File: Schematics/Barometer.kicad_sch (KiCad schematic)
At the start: 4 parts, among them U6 MPL3115A2R1

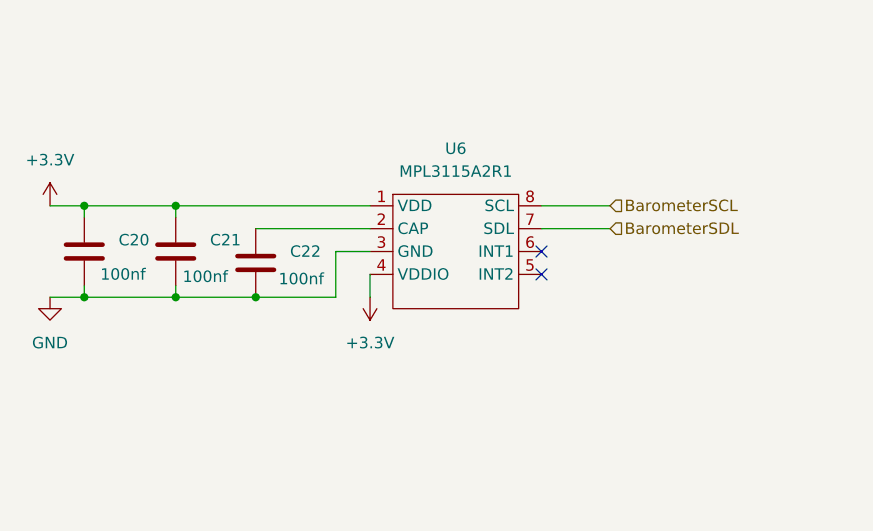
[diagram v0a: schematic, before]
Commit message: added aux pyro added reverse polarity protection re routed just need to clean up and check pin assignments
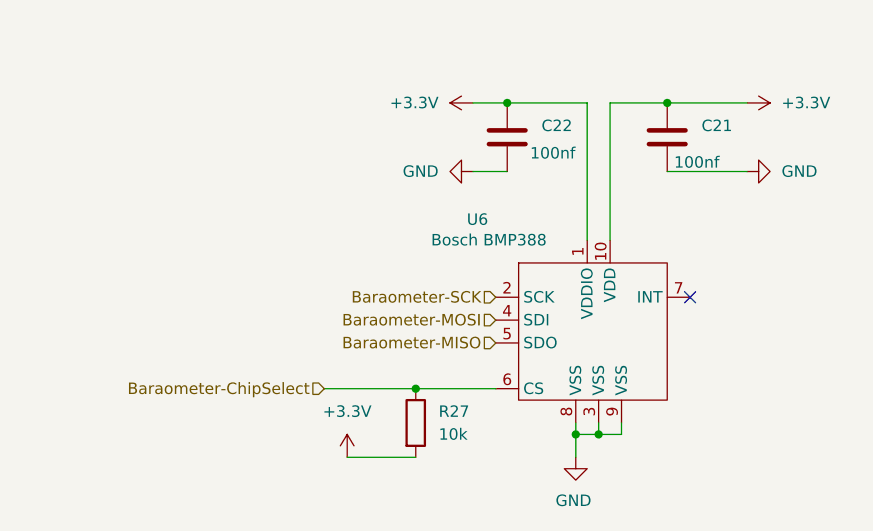
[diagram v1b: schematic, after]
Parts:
- removed C20: 100nf, Capacitor_SMD:C_0805_2012Metric_Pad1.18x1.45mm_HandSolder, symbol Device:C
- added R27: 10k, Resistor_SMD:R_0805_2012Metric_Pad1.20x1.40mm_HandSolder, symbol Device:R
- U6: value MPL3115A2R1 -> Bosch BMP388; footprint Package_LGA:LGA-8_3x5mm_P1.25mm -> myFootprints:PQFN50P200X200X80-10N; LCSC C54429 -> C779278
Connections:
- net BarometerSCL is gone; now on net GND: U6.8 (VSS)
- net +3.3V: now also C22.1, U6.10 (VDD), R27.2; no longer U6.4 (VDDIO)
- net GND: now also U6.9 (VSS)
- net Baraometer-SCK: now reaches U6.2 (SCK)
- net Baraometer-SCK: no longer C22.1
- net Baraometer-MISO: now reaches U6.5 (SDO)
- net Baraometer-ChipSelect: now reaches U6.6 (CS)
- net Baraometer-ChipSelect: now also R27.1
- net BarometerSDL: no longer names the net of U6.7 (INT)
- new net Baraometer-MOSI: U6.4 (SDI)
- no-connect marks 2 -> 1
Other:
- moved on the sheet: C21, C22

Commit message: added comments, awaiting review
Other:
- note added: "Baraometer to detect altitude and apogee events"
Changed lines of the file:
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@@
 	(generator_version "9.0")
 	(paper "A4")
+	(text "Baraometer to detect altitude and apogee events"
+		(exclude_from_sim no)
+		(at 157.48 56.896 0)
+		(effects
+			(font
+				(size 1.27 1.27)
+			)
+		)
+	)
 	(junction
 		(at 137.16 96.52)

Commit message: updated to KiCad 10.0, updated .gitignore
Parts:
- R27: LCSC C84376 -> C17414
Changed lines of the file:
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@@
 			)
 		)
-		(property "LCSC" "C84376"
+		(property "LCSC" "C17414"
 			(at 137.16 100.33 0)
 			(effects
